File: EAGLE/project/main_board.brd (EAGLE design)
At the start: 85 x 56 mm, 12 parts

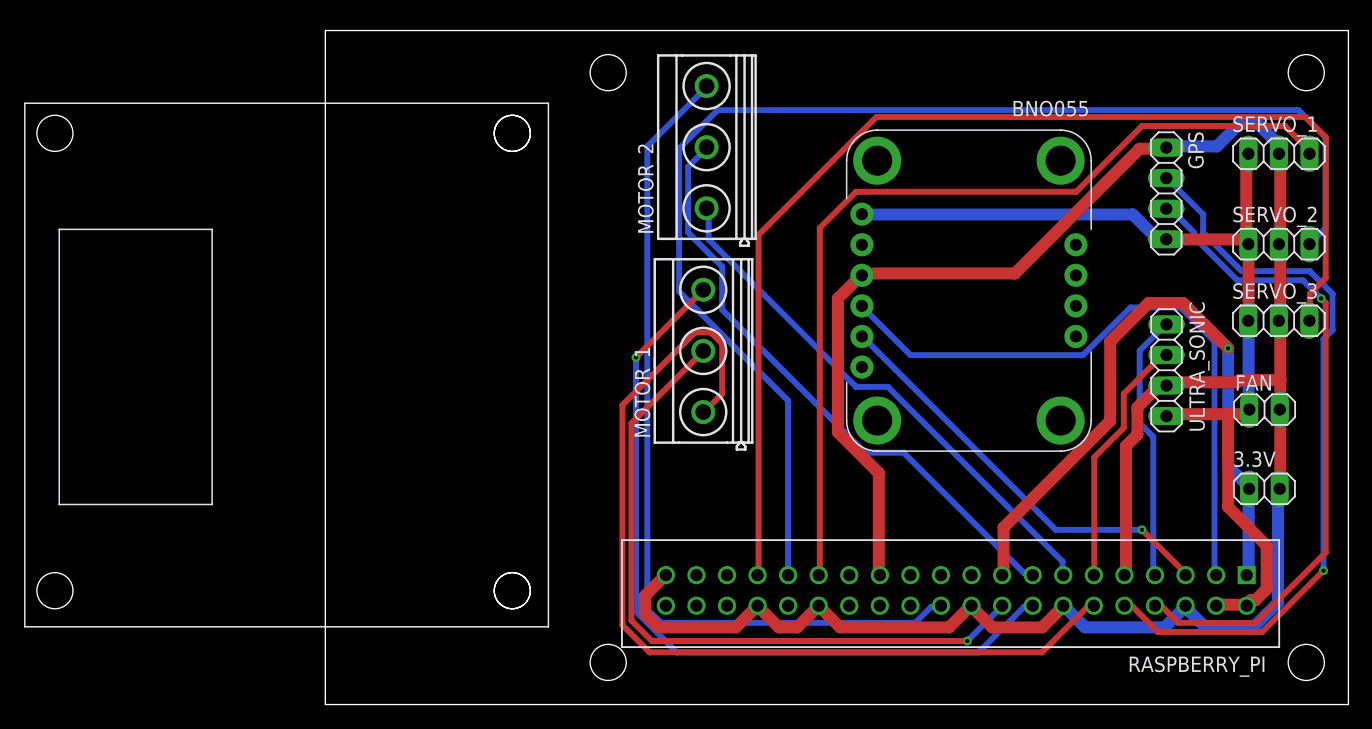
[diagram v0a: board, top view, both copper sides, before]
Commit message: add communication and temp/humid sensor module
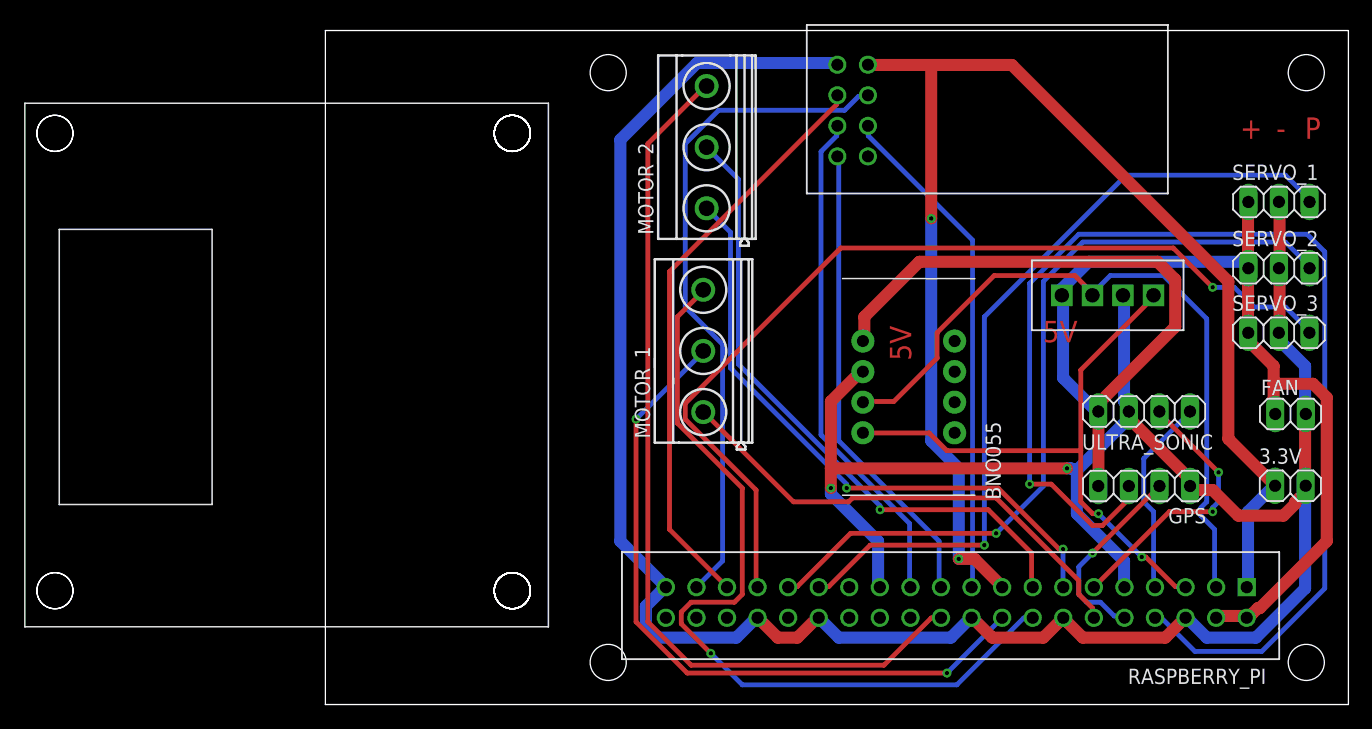
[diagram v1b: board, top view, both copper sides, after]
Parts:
- added NRF24L1: NRF24L01, nRF24L01:NRF24L01
- added U$1: DHT20, DHT20:DHT20
- moved GPS 24.4 mm to (-17.0, 18.2), turned to 180 degrees
- moved BNO055 9.43 mm to (-36.5, 26.4)
- moved SERVO_1 4.00 mm to (-5.77, 41.8)
- moved ULTRA_SONIC 3.90 mm to (-17.0, 24.3), turned to 0 degrees
- moved FAN 2.19 mm to (-4.81, 24.1)
- moved 3.3V 2.17 mm to (-4.82, 18.2)
- moved SERVO_2 2.00 mm to (-5.77, 36.3)
- moved RASPBERRY_PI 1.00 mm to (-42.6, 33.0)
- moved SERVO_3 1.00 mm to (-5.78, 30.9)
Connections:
- removed net 3VO: BNO055.2
- new net N$1: NRF24L1.CE, RASPBERRY_PI.35
- new net N$2: NRF24L1.CSN, RASPBERRY_PI.37
- new net N$3: NRF24L1.SCK, RASPBERRY_PI.23
- new net N$4: NRF24L1.MOSI, RASPBERRY_PI.19
- new net N$5: NRF24L1.MISO, RASPBERRY_PI.21
- net 3.3V: now also NRF24L1.VCC
- net 5V: now also BNO055.VIN, U$1.5V; no longer BNO055.1
- net BNO055_SCL: now also BNO055.SCL, U$1.SCL; no longer BNO055.5
- net BNO055_SDA: now also BNO055.SDA, U$1.SDA; no longer BNO055.4
- net GND: now also BNO055.GND, NRF24L1.GND, U$1.GND; no longer BNO055.3
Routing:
- net 3.3V: track 55.4 -> 112.0 mm, vias 1 -> 2
- net N$2: track 0.00 -> 55.9 mm
- net GND: track 198.7 -> 249.8 mm, vias 0 -> 2
- net N$1: track 0.00 -> 48.6 mm
- net RX: track 54.7 -> 100.6 mm
- net TX: track 61.5 -> 16.4 mm
- net 5V: track 82.5 -> 126.0 mm
- net N$3: track 0.00 -> 42.0 mm
- net N$4: track 0.00 -> 42.0 mm
- net N$5: track 0.00 -> 39.4 mm
- net PWM_SERVO_2: track 104.6 -> 66.3 mm, vias 0 -> 1
- net ENA: track 77.5 -> 40.9 mm
- net PWM_SERVO_3: track 96.0 -> 78.2 mm, vias 0 -> 1
- net BNO055_SCL: track 35.2 -> 50.0 mm, vias 1 -> 2
- net BNO055_SDA: track 53.3 -> 60.5 mm
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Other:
- board text added: "+"
- board text added: "-"
- board text added: "5V"
- board text added: "P"
